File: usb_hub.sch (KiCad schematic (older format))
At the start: 27 parts, among them U1 USB2514B_Bi, Y1 24MHz

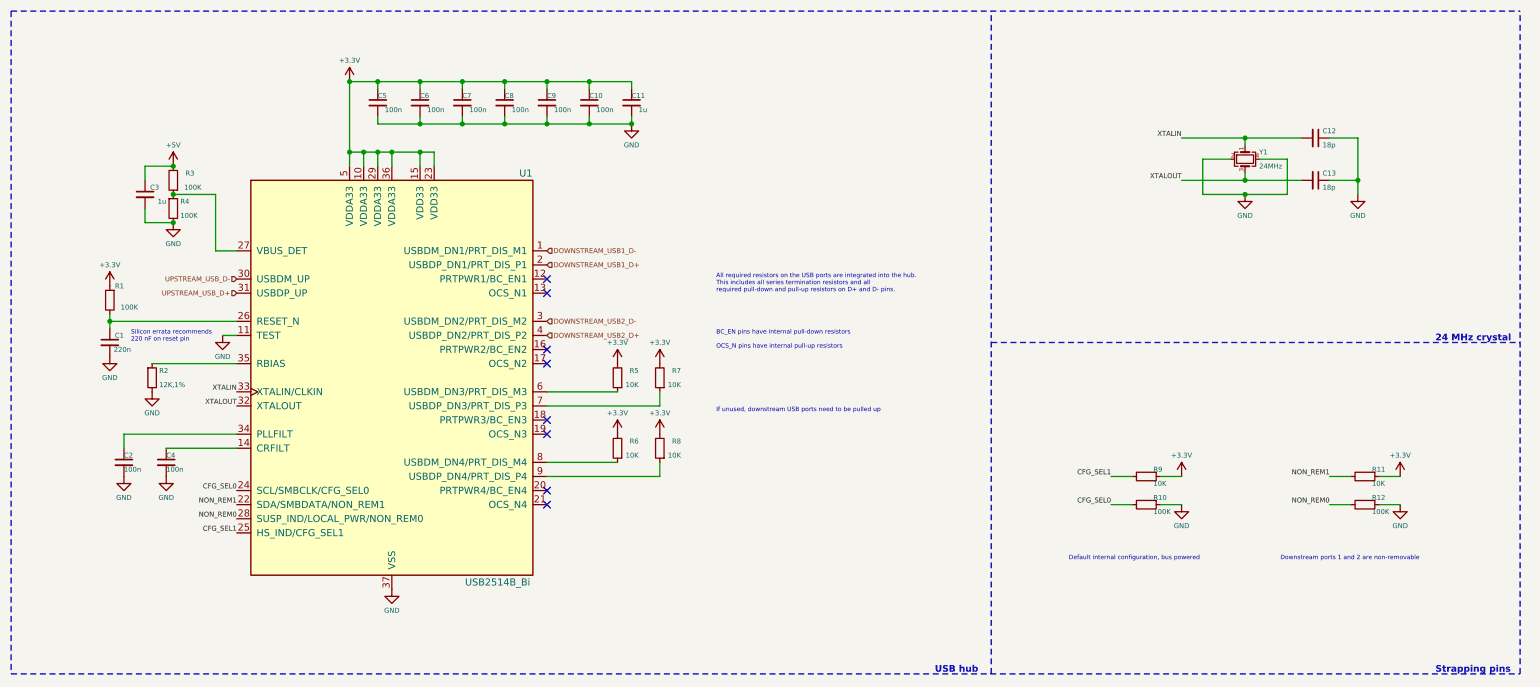
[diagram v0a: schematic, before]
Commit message: Use ESP32-C3-WROOM-02 module
Signed-off-by: Tomislav Milkovic <tomislav.milkovic95@gmail.com>
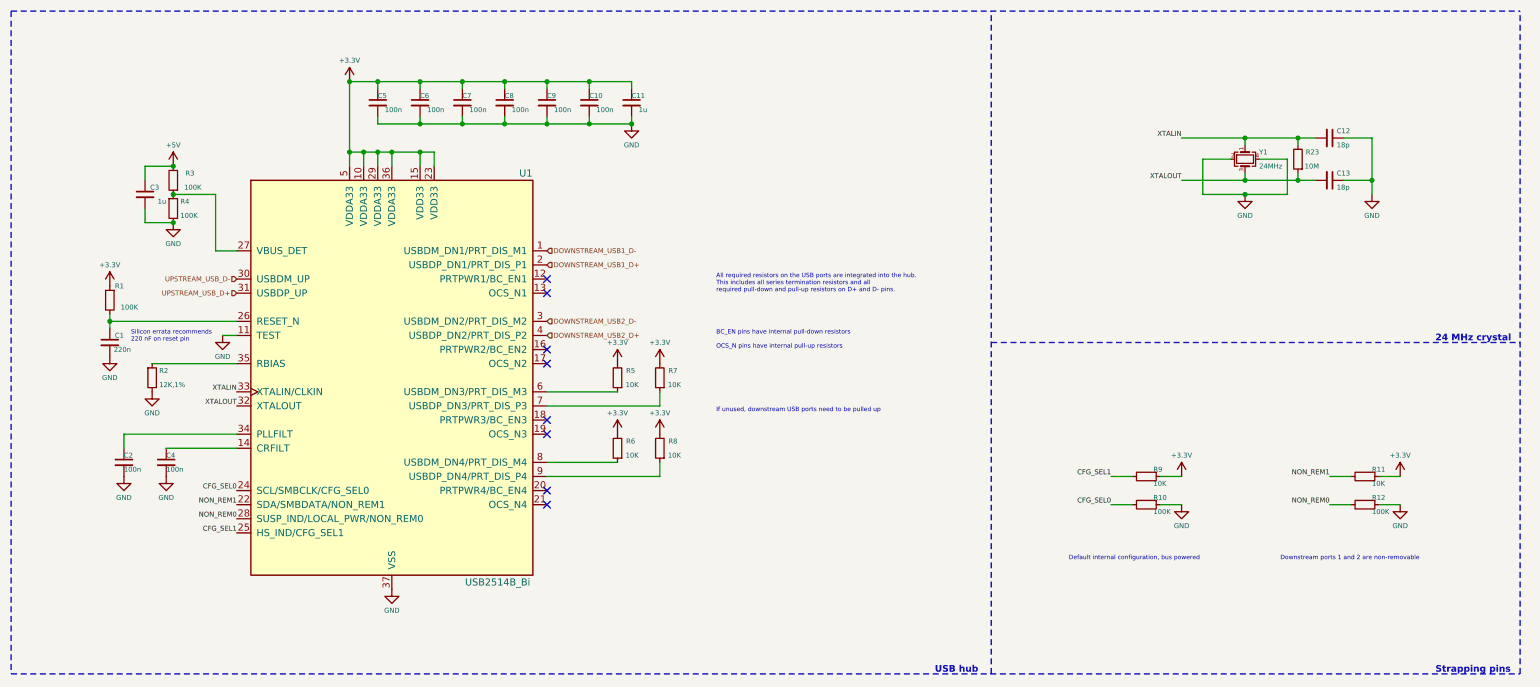
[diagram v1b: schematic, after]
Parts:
- added R23: 10M, Resistor_SMD:R_0402_1005Metric, symbol Device:R_Small
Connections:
- net XTALIN: now also R23.2
- net XTALOUT: now also R23.1
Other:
- moved on the sheet: C12, C13
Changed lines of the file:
@@
 AR Path="/637E103C" Ref="R?"  Part="1"
 AR Path="/637ACF0F/637E103C" Ref="R6"  Part="1"
-F 0 "R6" H 4650 3550 35  0000 L CNN
+F 0 "R6" H 4675 3550 35  0000 L CNN
 F 1 "10K" H 4650 3650 35  0000 L CNN
 F 2 "Resistor_SMD:R_0402_1005Metric" H 4800 3600 50  0001 C CNN
@@
 AR Path="/637E1043" Ref="R?"  Part="1"
 AR Path="/637ACF0F/637E1043" Ref="R8"  Part="1"
-F 0 "R8" H 4950 3550 35  0000 L CNN
+F 0 "R8" H 4975 3550 35  0000 L CNN
 F 1 "10K" H 4950 3650 35  0000 L CNN
 F 2 "Resistor_SMD:R_0402_1005Metric" H 5100 3600 50  0001 C CNN
@@
 AR Path="/637E104C" Ref="R?"  Part="1"
 AR Path="/637ACF0F/637E104C" Ref="R5"  Part="1"
-F 0 "R5" H 4650 3050 35  0000 L CNN
+F 0 "R5" H 4675 3050 35  0000 L CNN
 F 1 "10K" H 4650 3150 35  0000 L CNN
 F 2 "Resistor_SMD:R_0402_1005Metric" H 4800 3100 50  0001 C CNN
@@
 AR Path="/637E1053" Ref="R?"  Part="1"
 AR Path="/637ACF0F/637E1053" Ref="R7"  Part="1"
-F 0 "R7" H 4950 3050 35  0000 L CNN
+F 0 "R7" H 4975 3050 35  0000 L CNN
 F 1 "10K" H 4950 3150 35  0000 L CNN
 F 2 "Resistor_SMD:R_0402_1005Metric" H 5100 3100 50  0001 C CNN
@@
 	8950 1550 8950 1800
 Wire Wire Line
-	10050 1700 10050 1800
-Wire Wire Line
-	10050 1400 10050 1700
-Connection ~ 10050 1700
-Wire Wire Line
-	9850 1700 10050 1700
-Wire Wire Line
-	9250 1700 9650 1700
+	10150 1700 10150 1800
+Wire Wire Line
+	10150 1400 10150 1700
+Connection ~ 10150 1700
+Wire Wire Line
+	9950 1700 10150 1700
 Wire Wire Line
 	9250 1700 8800 1700
@@
 	9250 1650 9250 1700
 Wire Wire Line
-	10050 1400 9850 1400
-Wire Wire Line
-	9250 1400 9650 1400
+	10150 1400 9950 1400
 Wire Wire Line
 	9250 1400 8800 1400
@@
 L power:GND #PWR?
 U 1 1 637F5071
-P 10050 1800
+P 10150 1800
 AR Path="/637F5071" Ref="#PWR?"  Part="1"
 AR Path="/637ACF0F/637F5071" Ref="#PWR019"  Part="1"
-F 0 "#PWR019" H 10050 1550 50  0001 C CNN
-F 1 "GND" H 10050 1650 35  0000 C CNN
-F 2 "" H 10050 1800 50  0001 C CNN
-F 3 "" H 10050 1800 50  0001 C CNN
-	1    10050 1800
+F 0 "#PWR019" H 10150 1550 50  0001 C CNN
+F 1 "GND" H 10150 1650 35  0000 C CNN
+F 2 "" H 10150 1800 50  0001 C CNN
+F 3 "" H 10150 1800 50  0001 C CNN
+	1    10150 1800
 	1    0    0    -1
 $EndComp
@@
 L Device:C_Small C?
 U 1 1 637F5078
-P 9750 1400
+P 9850 1400
 AR Path="/637F5078" Ref="C?"  Part="1"
 AR Path="/637ACF0F/637F5078" Ref="C12"  Part="1"
-F 0 "C12" V 9700 1450 35  0000 L CNN
-F 1 "18p" V 9800 1450 35  0000 L CNN
-F 2 "Capacitor_SMD:C_0402_1005Metric" H 9750 1400 50  0001 C CNN
-F 3 "https://datasheet.lcsc.com/lcsc/1810191222_Samsung-Electro-Mechanics-CL05B104KB54PNC_C307331.pdf" H 9750 1400 50  0001 C CNN
-F 4 "C307331" H 9750 1400 50  0001 C CNN "LCSC"
-	1    9750 1400
+F 0 "C12" V 9800 1450 35  0000 L CNN
+F 1 "18p" V 9900 1450 35  0000 L CNN
+F 2 "Capacitor_SMD:C_0402_1005Metric" H 9850 1400 50  0001 C CNN
+F 3 "https://datasheet.lcsc.com/lcsc/1810191222_Samsung-Electro-Mechanics-CL05B104KB54PNC_C307331.pdf" H 9850 1400 50  0001 C CNN
+F 4 "C307331" H 9850 1400 50  0001 C CNN "LCSC"
+	1    9850 1400
 	0    1    1    0
 $EndComp
@@
 L Device:C_Small C?
 U 1 1 637F507F
-P 9750 1700
+P 9850 1700
 AR Path="/637F507F" Ref="C?"  Part="1"
 AR Path="/637ACF0F/637F507F" Ref="C13"  Part="1"
-F 0 "C13" V 9700 1750 35  0000 L CNN
-F 1 "18p" V 9800 1750 35  0000 L CNN
-F 2 "Capacitor_SMD:C_0402_1005Metric" H 9750 1700 50  0001 C CNN
-F 3 "https://datasheet.lcsc.com/lcsc/1810191222_Samsung-Electro-Mechanics-CL05B104KB54PNC_C307331.pdf" H 9750 1700 50  0001 C CNN
-F 4 "C307331" H 9750 1700 50  0001 C CNN "LCSC"
-	1    9750 1700
+F 0 "C13" V 9800 1750 35  0000 L CNN
+F 1 "18p" V 9900 1750 35  0000 L CNN
+F 2 "Capacitor_SMD:C_0402_1005Metric" H 9850 1700 50  0001 C CNN
+F 3 "https://datasheet.lcsc.com/lcsc/1810191222_Samsung-Electro-Mechanics-CL05B104KB54PNC_C307331.pdf" H 9850 1700 50  0001 C CNN
+F 4 "C307331" H 9850 1700 50  0001 C CNN "LCSC"
+	1    9850 1700
 	0    1    1    0
 $EndComp
@@
 Text Notes 9500 4400 0    31   ~ 0
 Downstream ports 1 and 2 are non-removable
+$Comp
+L Device:R_Small R?
+U 1 1 67B5B2FA
+P 9625 1550
+AR Path="/67B5B2FA" Ref="R?"  Part="1"
+AR Path="/637ACF0F/67B5B2FA" Ref="R23"  Part="1"
+F 0 "R23" H 9475 1500 35  0000 L CNN
+F 1 "10M" H 9475 1600 35  0000 L CNN
+F 2 "Resistor_SMD:R_0402_1005Metric" H 9625 1550 50  0001 C CNN
+F 3 "https://datasheet.lcsc.com/lcsc/2206010130_UNI-ROYAL-Uniroyal-Elec-0603WAF1001T5E_C21190.pdf" H 9625 1550 50  0001 C CNN
+F 4 "C21190" H 9625 1550 50  0001 C CNN "LCSC"
+	1    9625 1550
+	-1   0    0    1
+$EndComp
+Wire Wire Line
+	9250 1400 9625 1400
+Wire Wire Line
+	9250 1700 9625 1700
+Wire Wire Line
+	9625 1650 9625 1700
+Connection ~ 9625 1700
+Wire Wire Line
+	9625 1700 9750 1700
+Wire Wire Line
+	9625 1450 9625 1400
+Connection ~ 9625 1400
+Wire Wire Line
+	9625 1400 9750 1400
 $EndSCHEMATC

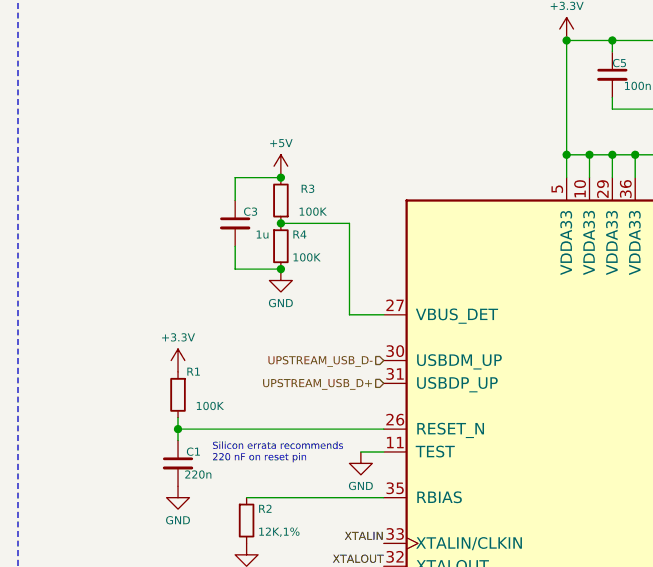
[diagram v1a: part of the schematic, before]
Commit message: Change USB UART adapter to CP2102
Signed-off-by: Tomislav Milkovic <tomislav.milkovic95@gmail.com>
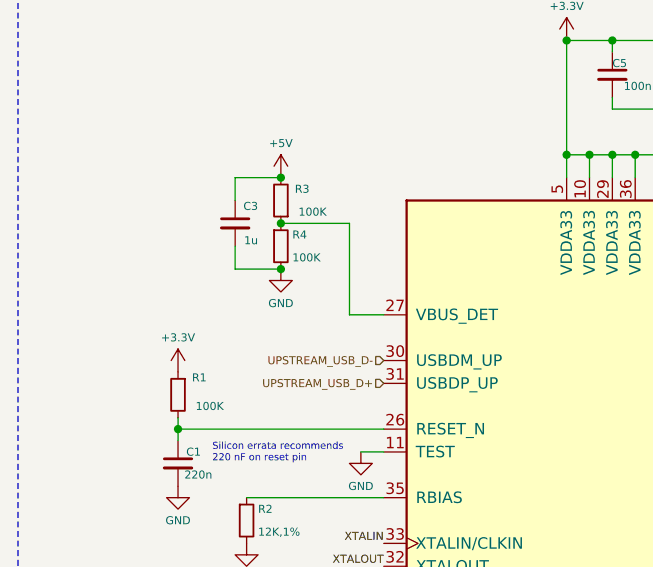
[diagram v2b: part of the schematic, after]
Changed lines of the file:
@@
 AR Path="/637E0FA2" Ref="R?"  Part="1"
 AR Path="/637ACF0F/637E0FA2" Ref="R3"  Part="1"
-F 0 "R3" H 1500 1650 35  0000 L CNN
+F 0 "R3" H 1525 1650 35  0000 L CNN
 F 1 "100K" H 1450 1750 35  0000 L CNN
 F 2 "Resistor_SMD:R_0402_1005Metric" H 1650 1700 50  0001 C CNN
@@
 AR Path="/637E0FA9" Ref="C?"  Part="1"
 AR Path="/637ACF0F/637E0FA9" Ref="C3"  Part="1"
-F 0 "C3" H 1350 1850 35  0000 L CNN
-F 1 "1u" H 1300 1750 35  0000 L CNN
+F 0 "C3" H 1350 1875 35  0000 L CNN
+F 1 "1u" H 1350 1725 35  0000 L CNN
 F 2 "Capacitor_SMD:C_0402_1005Metric" H 1450 1800 50  0001 C CNN
 F 3 "https://datasheet.lcsc.com/lcsc/1811091611_Samsung-Electro-Mechanics-CL05A105KA5NQNC_C52923.pdf" H 1450 1800 50  0001 C CNN
@@
 AR Path="/637E0FD0" Ref="R?"  Part="1"
 AR Path="/637ACF0F/637E0FD0" Ref="R1"  Part="1"
-F 0 "R1" H 1100 2650 35  0000 L CNN
+F 0 "R1" H 1075 2625 35  0000 L CNN
 F 1 "100K" H 1000 2500 35  0000 L CNN
 F 2 "Resistor_SMD:R_0402_1005Metric" H 1200 2550 50  0001 C CNN

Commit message: Add LCSC part numbers for all components
Signed-off-by: Tomislav Milkovic <tomislav.milkovic95@gmail.com>
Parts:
- removed C3: 1u, Capacitor_SMD:C_0402_1005Metric, symbol Device:C_Small
- removed R23: 10M, Resistor_SMD:R_0402_1005Metric, symbol Device:R_Small
- C1: LCSC C52923 -> C16772
- C11: value 1u -> 10u; LCSC C1779 -> C19702
- C12, C13: value 18p -> 6p8; LCSC C307331 -> C1576
- R1: LCSC C25744 -> C25741
- R10, R12, R3, R4: LCSC C21190 -> C25741
- R11, R9: value 10K -> 100K; LCSC C21190 -> C25741
- R2: LCSC C21190 -> C25752
- R5, R6, R7, R8: LCSC C21190 -> C25744
- Y1: LCSC (none) -> C194420
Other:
- note added: "C = 2 x Cload - Cstray"
- note added: "Crystal load capacitance: 6 pF\nCrystal accuracy: +-35 ppm"
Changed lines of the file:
@@
 Sheet 2 5
 Title "USB hub"
-Date "2022-11-20"
+Date "2025-02-16"
 Rev "1.0"
 Comp "Copyright: Tomislav Milkovic"
@@
 AR Path="/637ACF0F/637E0F34" Ref="C11"  Part="1"
 F 0 "C11" H 4900 1200 35  0000 L CNN
-F 1 "1u" H 4950 1100 35  0000 L CNN
+F 1 "10u" H 4925 1100 35  0000 L CNN
 F 2 "Capacitor_SMD:C_0603_1608Metric" H 4900 1150 50  0001 C CNN
 F 3 "https://datasheet.lcsc.com/lcsc/2004251506_Murata-Electronics-GRM21BR61H106KE43L_C440198.pdf" H 4900 1150 50  0001 C CNN
-F 4 "C1779" H 4900 1150 50  0001 C CNN "LCSC"
+F 4 "C19702" H 4900 1150 50  0001 C CNN "LCSC"
 	1    4900 1150
 	1    0    0    -1
@@
 F 2 "Resistor_SMD:R_0402_1005Metric" H 8550 4000 50  0001 C CNN
 F 3 "https://datasheet.lcsc.com/lcsc/2206010130_UNI-ROYAL-Uniroyal-Elec-0603WAF1001T5E_C21190.pdf" H 8550 4000 50  0001 C CNN
-F 4 "C21190" H 8550 4000 50  0001 C CNN "LCSC"
+F 4 "C25741" H 8550 4000 50  0001 C CNN "LCSC"
 	1    8550 4000
 	0    1    1    0
@@
 F 2 "Resistor_SMD:R_0402_1005Metric" H 1650 1900 50  0001 C CNN
 F 3 "https://datasheet.lcsc.com/lcsc/2206010130_UNI-ROYAL-Uniroyal-Elec-0603WAF1001T5E_C21190.pdf" H 1650 1900 50  0001 C CNN
-F 4 "C21190" H 1650 1900 50  0001 C CNN "LCSC"
+F 4 "C25741" H 1650 1900 50  0001 C CNN "LCSC"
 	1    1650 1900
 	1    0    0    -1
@@
 F 2 "Resistor_SMD:R_0402_1005Metric" H 1650 1700 50  0001 C CNN
 F 3 "https://datasheet.lcsc.com/lcsc/2206010130_UNI-ROYAL-Uniroyal-Elec-0603WAF1001T5E_C21190.pdf" H 1650 1700 50  0001 C CNN
-F 4 "C21190" H 1650 1700 50  0001 C CNN "LCSC"
+F 4 "C25741" H 1650 1700 50  0001 C CNN "LCSC"
 	1    1650 1700
 	-1   0    0    1
-$EndComp
-$Comp
-L Device:C_Small C?
-U 1 1 637E0FA9
-P 1450 1800
-AR Path="/637E0FA9" Ref="C?"  Part="1"
-AR Path="/637ACF0F/637E0FA9" Ref="C3"  Part="1"
-F 0 "C3" H 1350 1875 35  0000 L CNN
-F 1 "1u" H 1350 1725 35  0000 L CNN
-F 2 "Capacitor_SMD:C_0402_1005Metric" H 1450 1800 50  0001 C CNN
-F 3 "https://datasheet.lcsc.com/lcsc/1811091611_Samsung-Electro-Mechanics-CL05A105KA5NQNC_C52923.pdf" H 1450 1800 50  0001 C CNN
-F 4 "C52923" H 1450 1800 50  0001 C CNN "LCSC"
-	1    1450 1800
-	-1   0    0    -1
 $EndComp
 Wire Wire Line
@@
 F 2 "Capacitor_SMD:C_0402_1005Metric" H 1200 2850 50  0001 C CNN
 F 3 "https://datasheet.lcsc.com/lcsc/1811091611_Samsung-Electro-Mechanics-CL05A105KA5NQNC_C52923.pdf" H 1200 2850 50  0001 C CNN
-F 4 "C52923" H 1200 2850 50  0001 C CNN "LCSC"
+F 4 "C16772" H 1200 2850 50  0001 C CNN "LCSC"
 	1    1200 2850
 	-1   0    0    -1
@@
 F 2 "Resistor_SMD:R_0402_1005Metric" H 1200 2550 50  0001 C CNN
 F 3 "https://datasheet.lcsc.com/lcsc/2206010100_UNI-ROYAL-Uniroyal-Elec-0402WGF1002TCE_C25744.pdf" H 1200 2550 50  0001 C CNN
-F 4 "C25744" H 1200 2550 50  0001 C CNN "LCSC"
+F 4 "C25741" H 1200 2550 50  0001 C CNN "LCSC"
 	1    1200 2550
 	-1   0    0    -1
@@
 F 2 "Resistor_SMD:R_0402_1005Metric" H 1500 3100 50  0001 C CNN
 F 3 "https://datasheet.lcsc.com/lcsc/2206010130_UNI-ROYAL-Uniroyal-Elec-0603WAF1001T5E_C21190.pdf" H 1500 3100 50  0001 C CNN
-F 4 "C21190" H 1500 3100 50  0001 C CNN "LCSC"
+F 4 "C25752" H 1500 3100 50  0001 C CNN "LCSC"
 	1    1500 3100
 	1    0    0    -1
@@
 Wire Wire Line
 	4300 3200 4800 3200
-Wire Wire Line
-	1450 1700 1450 1600
-Wire Wire Line
-	1450 1600 1650 1600
-Connection ~ 1650 1600
-Wire Wire Line
-	1450 1900 1450 2000
-Wire Wire Line
-	1450 2000 1650 2000
-Connection ~ 1650 2000
 Text Notes 1350 2850 0    31   ~ 0
 Silicon errata recommends\n220 nF on reset pin
@@
 AR Path="/637ACF0F/637E1007" Ref="R9"  Part="1"
 F 0 "R9" V 8500 3850 35  0000 L CNN
-F 1 "10K" V 8600 3850 35  0000 L CNN
+F 1 "100K" V 8600 3850 35  0000 L CNN
 F 2 "Resistor_SMD:R_0402_1005Metric" H 8550 3800 50  0001 C CNN
 F 3 "https://datasheet.lcsc.com/lcsc/2206010130_UNI-ROYAL-Uniroyal-Elec-0603WAF1001T5E_C21190.pdf" H 8550 3800 50  0001 C CNN
-F 4 "C21190" H 8550 3800 50  0001 C CNN "LCSC"
+F 4 "C25741" H 8550 3800 50  0001 C CNN "LCSC"
 	1    8550 3800
 	0    1    1    0
@@
 F 2 "Resistor_SMD:R_0402_1005Metric" H 10100 4000 50  0001 C CNN
 F 3 "https://datasheet.lcsc.com/lcsc/2206010130_UNI-ROYAL-Uniroyal-Elec-0603WAF1001T5E_C21190.pdf" H 10100 4000 50  0001 C CNN
-F 4 "C21190" H 10100 4000 50  0001 C CNN "LCSC"
+F 4 "C25741" H 10100 4000 50  0001 C CNN "LCSC"
 	1    10100 4000
 	0    1    1    0
@@
 AR Path="/637ACF0F/637E1025" Ref="R11"  Part="1"
 F 0 "R11" V 10050 3850 35  0000 L CNN
-F 1 "10K" V 10150 3850 35  0000 L CNN
+F 1 "100K" V 10150 3850 35  0000 L CNN
 F 2 "Resistor_SMD:R_0402_1005Metric" H 10100 3800 50  0001 C CNN
 F 3 "https://datasheet.lcsc.com/lcsc/2206010130_UNI-ROYAL-Uniroyal-Elec-0603WAF1001T5E_C21190.pdf" H 10100 3800 50  0001 C CNN
-F 4 "C21190" H 10100 3800 50  0001 C CNN "LCSC"
+F 4 "C25741" H 10100 3800 50  0001 C CNN "LCSC"
 	1    10100 3800
 	0    1    1    0
@@
 F 2 "Resistor_SMD:R_0402_1005Metric" H 4800 3600 50  0001 C CNN
 F 3 "https://datasheet.lcsc.com/lcsc/2206010130_UNI-ROYAL-Uniroyal-Elec-0603WAF1001T5E_C21190.pdf" H 4800 3600 50  0001 C CNN
-F 4 "C21190" H 4800 3600 50  0001 C CNN "LCSC"
+F 4 "C25744" H 4800 3600 50  0001 C CNN "LCSC"
 	1    4800 3600
 	-1   0    0    1
@@
 F 2 "Resistor_SMD:R_0402_1005Metric" H 5100 3600 50  0001 C CNN
 F 3 "https://datasheet.lcsc.com/lcsc/2206010130_UNI-ROYAL-Uniroyal-Elec-0603WAF1001T5E_C21190.pdf" H 5100 3600 50  0001 C CNN
-F 4 "C21190" H 5100 3600 50  0001 C CNN "LCSC"
+F 4 "C25744" H 5100 3600 50  0001 C CNN "LCSC"
 	1    5100 3600
 	-1   0    0    1
@@
 F 2 "Resistor_SMD:R_0402_1005Metric" H 4800 3100 50  0001 C CNN
 F 3 "https://datasheet.lcsc.com/lcsc/2206010130_UNI-ROYAL-Uniroyal-Elec-0603WAF1001T5E_C21190.pdf" H 4800 3100 50  0001 C CNN
-F 4 "C21190" H 4800 3100 50  0001 C CNN "LCSC"
+F 4 "C25744" H 4800 3100 50  0001 C CNN "LCSC"
 	1    4800 3100
 	-1   0    0    1
@@
 F 2 "Resistor_SMD:R_0402_1005Metric" H 5100 3100 50  0001 C CNN
 F 3 "https://datasheet.lcsc.com/lcsc/2206010130_UNI-ROYAL-Uniroyal-Elec-0603WAF1001T5E_C21190.pdf" H 5100 3100 50  0001 C CNN
-F 4 "C21190" H 5100 3100 50  0001 C CNN "LCSC"
+F 4 "C25744" H 5100 3100 50  0001 C CNN "LCSC"
 	1    5100 3100
 	-1   0    0    1
@@
 AR Path="/637ACF0F/637F5078" Ref="C12"  Part="1"
 F 0 "C12" V 9800 1450 35  0000 L CNN
-F 1 "18p" V 9900 1450 35  0000 L CNN
+F 1 "6p8" V 9900 1450 35  0000 L CNN
 F 2 "Capacitor_SMD:C_0402_1005Metric" H 9850 1400 50  0001 C CNN
 F 3 "https://datasheet.lcsc.com/lcsc/1810191222_Samsung-Electro-Mechanics-CL05B104KB54PNC_C307331.pdf" H 9850 1400 50  0001 C CNN
-F 4 "C307331" H 9850 1400 50  0001 C CNN "LCSC"
+F 4 "C1576" H 9850 1400 50  0001 C CNN "LCSC"
 	1    9850 1400
 	0    1    1    0
@@
 AR Path="/637ACF0F/637F507F" Ref="C13"  Part="1"
 F 0 "C13" V 9800 1750 35  0000 L CNN
-F 1 "18p" V 9900 1750 35  0000 L CNN
+F 1 "6p8" V 9900 1750 35  0000 L CNN
 F 2 "Capacitor_SMD:C_0402_1005Metric" H 9850 1700 50  0001 C CNN
 F 3 "https://datasheet.lcsc.com/lcsc/1810191222_Samsung-Electro-Mechanics-CL05B104KB54PNC_C307331.pdf" H 9850 1700 50  0001 C CNN
-F 4 "C307331" H 9850 1700 50  0001 C CNN "LCSC"
+F 4 "C1576" H 9850 1700 50  0001 C CNN "LCSC"
 	1    9850 1700
 	0    1    1    0
@@
 AR Path="/637ACF0F/637F508E" Ref="Y1"  Part="1"
 F 0 "Y1" V 9200 1650 35  0000 L CNN
-F 1 "24MHz" V 9300 1650 35  0000 L CNN
+F 1 "24MHz" V 9325 1625 35  0000 L CNN
 F 2 "Crystal:Crystal_SMD_2016-4Pin_2.0x1.6mm" H 9250 1550 50  0001 C CNN
-F 3 "~" H 9250 1550 50  0001 C CNN
+F 3 "https://www.lcsc.com/datasheet/lcsc_datasheet_2304140030_Murata-Electronics-XRCGB24M000F3A00R0_C194420.pdf" H 9250 1550 50  0001 C CNN
+F 4 "C194420" V 9250 1550 50  0001 C CNN "LCSC"
 	1    9250 1550
 	0    1    1    0
@@
 Text Notes 9500 4400 0    31   ~ 0
 Downstream ports 1 and 2 are non-removable
-$Comp
-L Device:R_Small R?
-U 1 1 67B5B2FA
-P 9625 1550
-AR Path="/67B5B2FA" Ref="R?"  Part="1"
-AR Path="/637ACF0F/67B5B2FA" Ref="R23"  Part="1"
-F 0 "R23" H 9475 1500 35  0000 L CNN
-F 1 "10M" H 9475 1600 35  0000 L CNN
-F 2 "Resistor_SMD:R_0402_1005Metric" H 9625 1550 50  0001 C CNN
-F 3 "https://datasheet.lcsc.com/lcsc/2206010130_UNI-ROYAL-Uniroyal-Elec-0603WAF1001T5E_C21190.pdf" H 9625 1550 50  0001 C CNN
-F 4 "C21190" H 9625 1550 50  0001 C CNN "LCSC"
-	1    9625 1550
-	-1   0    0    1
-$EndComp
-Wire Wire Line
-	9250 1400 9625 1400
-Wire Wire Line
-	9250 1700 9625 1700
-Wire Wire Line
-	9625 1650 9625 1700
-Connection ~ 9625 1700
-Wire Wire Line
-	9625 1700 9750 1700
-Wire Wire Line
-	9625 1450 9625 1400
-Connection ~ 9625 1400
-Wire Wire Line
-	9625 1400 9750 1400
+Wire Wire Line
+	9250 1400 9750 1400
+Wire Wire Line
+	9250 1700 9750 1700
+Text Notes 10200 1575 0    35   ~ 0
+C = 2 x Cload - Cstray
+Text Notes 8875 2150 0    35   ~ 0
+Crystal load capacitance: 6 pF\nCrystal accuracy: +-35 ppm
 $EndSCHEMATC

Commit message: PCB: Rough component placement done
Signed-off-by: Tomislav Milkovic <tomislav.milkovic95@gmail.com>
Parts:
- renumbered C1 to C10, C2 to C11, C4 to C12, C12 to C13, C13 to C14, C5 to C3, C6 to C4, C7 to C5, C8 to C6, C9 to C7, C10 to C8, C11 to C9, R6 to R10, R8 to R11, R10 to R12, R9 to R13, R12 to R14, R11 to R15, R3 to R4, R4 to R5, R1 to R6, R2 to R7, R5 to R8, R7 to R9, U1 to U3
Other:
- moved on the sheet: R12, R13, R14, R15
